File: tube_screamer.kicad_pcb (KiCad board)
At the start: 2 copper layers, 80 x 90 mm, 51 parts, among them J1 NMJ6HHD2, J2 NMJ6HHD2, J3 Conn_01x05, J4 Conn_01x05, J5 Conn_01x05, Q1 MMBT5551, Q2 MMBT5551, Q3 MMBT5551, SW1 SW_DPDT_x2, U1 NE5532

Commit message: Goin well.
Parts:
- removed TP11: input, TestPoint:TestPoint_THTPad_2.5x2.5mm_Drill1.2mm
- removed TP12: ground, TestPoint:TestPoint_THTPad_2.5x2.5mm_Drill1.2mm
- added BT1: Battery_Cell, pedale:BatteryHolder_Eagle_12BH611-GR, F.Cu at (70.8, 89.7)
- added D5: 1N4148WS, Diode_SMD:D_SOD-323, F.Cu at (35.5, 92.0)
- added D8: floating_green_led, pedale:floating_green_led, F.Cu at (74.0, 138.0)
- added D9: floating_red_led, pedale:floating_red_led, F.Cu at (106.0, 138.0)
- added H1: MountingHole, pedale:M3_hole_with_spacer, F.Cu at (55.0, 55.0)
- added H2: MountingHole, pedale:M3_hole_with_spacer, F.Cu at (125.0, 55.0)
- added H3: MountingHole, pedale:M3_hole_with_spacer, F.Cu at (55.0, 145.0)
- added H4: MountingHole, pedale:M3_hole_with_spacer, F.Cu at (90.0, 145.0)
- added H5: MountingHole, pedale:M3_hole_with_spacer, F.Cu at (125.0, 145.0)
- added J6: Barrel_Jack_MountingPin, Connector_BarrelJack:BarrelJack_GCT_DCJ200-10-A_Horizontal, F.Cu at (63.9, 103.3)
- added P1: tube_screamer_front_panel, pedale:tube_screamer_front_plate, F.Cu at (50.0, 50.0)
- added RV1: floating_pot_knob, pedale:floating_pot_knob, F.Cu at (34.4, 102.2)
- added RV5: floating_pot, pedale:floating_pot, F.Cu at (34.4, 100.7)
- added RV6: floating_pot, pedale:floating_pot, F.Cu at (32.9, 102.2)
- added RV7: floating_pot_knob, pedale:floating_pot_knob, F.Cu at (32.9, 100.7)
- added RV8: floating_pot, pedale:floating_pot, F.Cu at (31.4, 102.2)
- added RV9: floating_pot_knob, pedale:floating_pot_knob, F.Cu at (31.4, 100.7)
- added SIM1: Logo_Open_Hardware_Small, Symbol:OSHW-Logo2_7.3x6mm_SilkScreen, F.Cu at (108.0, 145.0)
- moved C11 70.7 mm to (97.4, 65.0)
- moved C6 70.7 mm to (95.4, 58.8)
- moved D3 70.7 mm to (112.8, 66.0)
- moved R19 70.7 mm to (87.4, 65.3)
- moved C1 70.7 mm to (64.3, 62.9)
- moved C10 70.7 mm to (63.5, 68.6)
- moved C14 70.7 mm to (124.0, 60.4)
- moved C16 70.7 mm to (115.6, 75.9)
- moved C17 70.7 mm to (124.9, 66.2)
- moved C18 70.7 mm to (108.6, 67.4)
- moved C3 70.7 mm to (68.0, 69.2)
- moved C5 70.7 mm to (72.0, 75.9)
- moved C9 70.7 mm to (55.7, 63.8)
- moved D1 70.7 mm to (68.0, 67.1)
- moved D2 70.7 mm to (68.0, 64.4)
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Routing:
- net Net-(D4-A): track 66.4 -> 68.7 mm
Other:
- board size 80 x 90 mm -> 80 x 100 mm

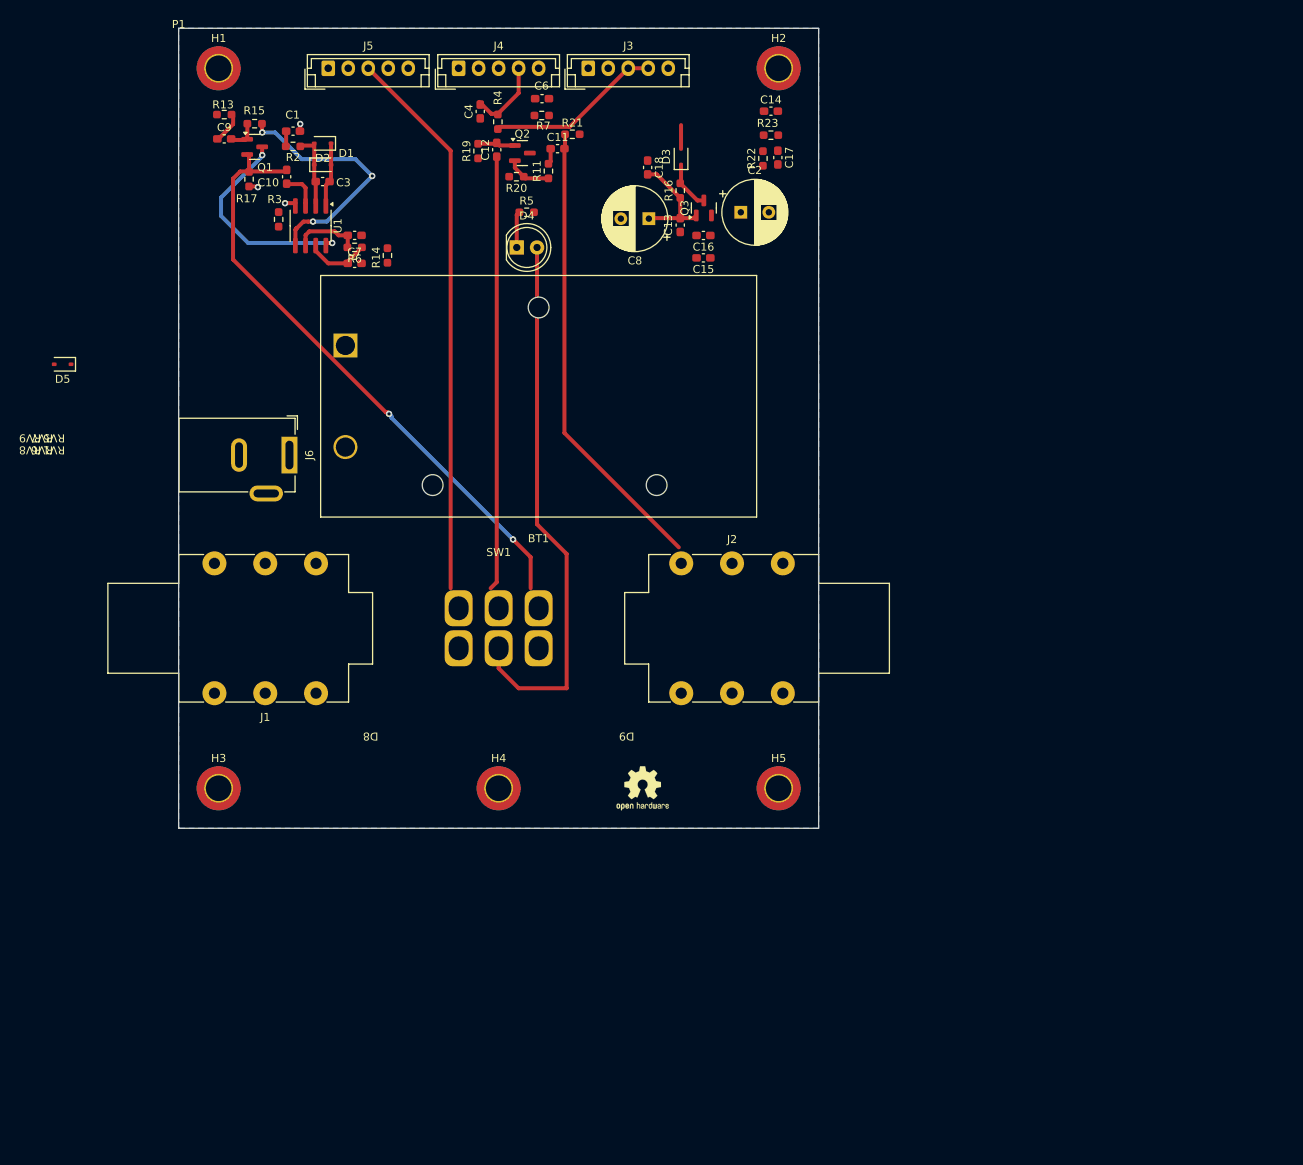
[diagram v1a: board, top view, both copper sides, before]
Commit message: 3D bodies
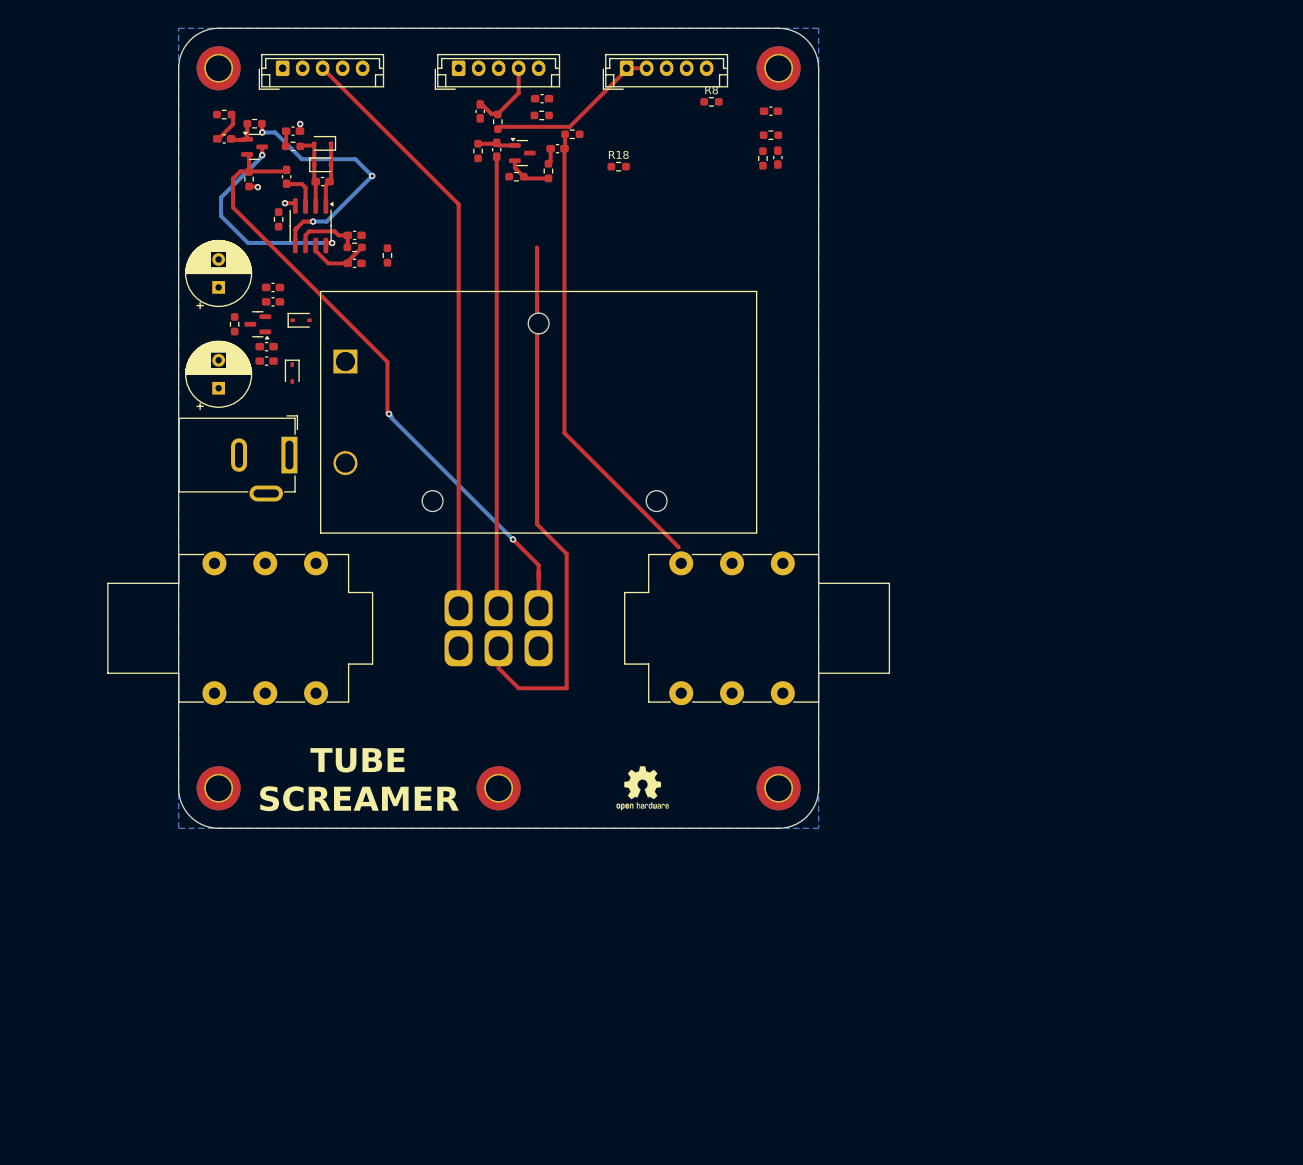
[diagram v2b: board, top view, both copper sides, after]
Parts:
- removed D4: LED, LED_THT:LED_D5.0mm
- removed R5: 1k, Resistor_SMD:R_0603_1608Metric_Pad0.98x0.95mm_HandSolder
- removed RV6: floating_pot, pedale:floating_pot
- added R18: 1k, Resistor_SMD:R_0603_1608Metric_Pad0.98x0.95mm_HandSolder, F.Cu at (105.0, 67.3)
- added R8: 1k, Resistor_SMD:R_0603_1608Metric_Pad0.98x0.95mm_HandSolder, F.Cu at (116.6, 59.2)
- moved RV1 87.4 mm to (112.0, 62.0), turned to 0 degrees
- moved C2 65.9 mm to (55.0, 82.4), turned to 90 degrees
- moved RV8 63.4 mm to (90.0, 78.0)
- moved RV7 61.8 mm to (90.0, 77.0), turned to 0 degrees
- moved R16 58.2 mm to (57.0, 87.0)
- moved C8 57.8 mm to (55.0, 95.0), turned to 90 degrees
- moved Q3 57.6 mm to (59.9, 87.0), turned to 180 degrees
- moved D3 55.6 mm to (64.2, 93.1), turned to -90 degrees
- moved C16 54.2 mm to (61.8, 82.4), turned to 0 degrees
- moved C15 54.1 mm to (61.8, 84.2), turned to 0 degrees
- moved C13 53.9 mm to (61.0, 89.8), turned to 0 degrees
- moved C18 53.4 mm to (61.0, 91.6), turned to 180 degrees
- moved RV9 53.3 mm to (68.0, 62.0), turned to 0 degrees
- moved RV5 50.5 mm to (68.0, 63.0), turned to 0 degrees
- moved D5 30.3 mm to (65.3, 86.5), turned to 0 degrees
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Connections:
- C4 pad 2: Net-(J4-Pin_4) -> Net-(J4-Pin_1)
- C5 pad 1: Net-(J4-Pin_4) -> Net-(J4-Pin_1)
- C5 pad 2: Net-(J4-Pin_2) -> Net-(J4-Pin_3)
- C6 pad 1: Net-(J4-Pin_3) -> Net-(J4-Pin_2)
- J3 pad 1: 0 -> Net-(D1-K)
- J3 pad 2: Net-(D1-K) -> Net-(D1-A)
- J3 pad 4: Net-(D1-A) -> 9V
- J3 pad 5: 0 -> Net-(J3-Pin_5)
- J4 pad 1: 0 -> Net-(J4-Pin_1)
- J4 pad 4: Net-(J4-Pin_4) -> unconnected-(J4-Pin_4-Pad4)
- J4 pad 5: 0 -> unconnected-(J4-Pin_5-Pad5)
- J5 pad 2: 0 -> /SW_ON
- J5 pad 3: /SW_ON -> Net-(J5-Pin_3)
- J5 pad 5: 0 -> Net-(J5-Pin_5)
- R14 pad 1: Net-(J5-Pin_4) -> Net-(J5-Pin_3)
- R4 pad 1: Net-(J4-Pin_4) -> Net-(J4-Pin_1)
- R6 pad 2: Net-(J4-Pin_2) -> Net-(J4-Pin_3)
- SW1 pad 5: Net-(D4-A) -> Net-(J5-Pin_4)
- U1 pad 6: Net-(J4-Pin_2) -> Net-(J4-Pin_3)
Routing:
- net Net-(J5-Pin_4): track 0.00 -> 68.7 mm
- net Net-(D4-A): track 68.7 -> 0.00 mm
- net Net-(Q3-B): track 13.9 -> 0.00 mm
- net Net-(J4-Pin_4): track 9.70 -> 0.00 mm
- net Net-(J4-Pin_1): track 0.00 -> 9.70 mm
- net Net-(J4-Pin_3): track 0.00 -> 8.17 mm
- net Net-(J4-Pin_2): track 8.17 -> 0.00 mm
- net Net-(D3-K): track 6.16 -> 0.00 mm
- net /SW_ON: track 69.3 -> 74.5 mm
- net Net-(D4-K): track 4.54 -> 0.00 mm
- net IN_BUFF: track 76.2 -> 80.0 mm
- net Net-(D3-A): track 2.90 -> 0.00 mm
- net /SW_MID: track 54.3 -> 56.5 mm
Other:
- outline, holes or cut-outs redrawn
- board text added: "TUBE SCREAMER"

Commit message: v1.
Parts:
- added RV6: floating_pot, pedale:floating_pot, F.Cu at (112.0, 63.0)
- moved R13 53.4 mm to (106.8, 76.5), turned to -90 degrees
- moved C7 50.3 mm to (119.2, 62.0), turned to 90 degrees
- moved C9 50.0 mm to (105.0, 72.6), turned to -90 degrees
- moved R6 48.7 mm to (119.2, 65.8), turned to -90 degrees
- moved R15 47.7 mm to (105.0, 76.3), turned to 90 degrees
- moved R3 47.3 mm to (109.5, 68.8), turned to 0 degrees
- moved U1 47.2 mm to (112.5, 64.2), turned to 0 degrees
- moved Q1 43.7 mm to (102.0, 75.1), turned to -90 degrees
- moved C10 41.7 mm to (105.2, 68.5), turned to 0 degrees
- moved R17 39.5 mm to (97.9, 74.4), turned to 180 degrees
- moved C3 38.2 mm to (105.8, 64.0), turned to 90 degrees
- moved C1 36.6 mm to (100.5, 68.7)
- moved R2 36.2 mm to (100.5, 66.8)
- moved D1 35.9 mm to (103.7, 64.0), turned to 90 degrees
- moved D2 33.2 mm to (101.2, 63.8), turned to -90 degrees
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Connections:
- net Net-(J5-Pin_3) renamed OP_OUT
- J1 pad S: unconnected-(J1-PadS) -> 0
- J2 pad S: unconnected-(J2-PadS) -> 0
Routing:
- net Net-(J1-PadT): track 0.00 -> 98.4 mm, vias 0 -> 2
- net Net-(J5-Pin_4): track 68.7 -> 126.2 mm
- net Net-(C7-Pad2): track 0.00 -> 54.3 mm, vias 0 -> 4
- net 4V5: track 31.2 -> 0.00 mm, vias 3 -> 0
- net 9V: track 26.9 -> 3.25 mm, vias 2 -> 1
- net IN_BUFF: track 80.0 -> 59.0 mm
- net Net-(Q3-B): track 0.00 -> 13.7 mm
- net Net-(D3-K): track 0.00 -> 13.6 mm
- net Net-(D1-K): track 9.08 -> 20.7 mm, vias 0 -> 1
- net Net-(D3-A): track 0.00 -> 9.34 mm
- net Net-(J4-Pin_3): track 8.17 -> 16.9 mm
- net Net-(D1-A): track 29.7 -> 37.6 mm
- net Net-(BT1-+): track 0.00 -> 7.01 mm
- net Net-(J4-Pin_1): track 9.70 -> 16.7 mm
- net Net-(J5-Pin_5): track 0.00 -> 6.49 mm
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
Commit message: v2.
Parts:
- moved R17 29.2 mm to (127.1, 74.9), turned to -90 degrees
- moved C7 28.1 mm to (93.1, 72.2), turned to -90 degrees
- moved R14 26.4 mm to (91.3, 72.3)
- moved R6 26.3 mm to (93.1, 68.7), turned to 90 degrees
- moved Q1 22.0 mm to (124.0, 74.8), turned to 180 degrees
- moved C17 21.3 mm to (97.0, 73.7)
- moved C9 21.3 mm to (125.3, 78.8), turned to 90 degrees
- moved C4 20.4 mm to (103.0, 74.7), turned to -90 degrees
- moved R15 17.7 mm to (122.6, 77.9), turned to 0 degrees
- moved R4 16.4 mm to (101.4, 74.7), turned to 90 degrees
- moved R13 16.2 mm to (122.6, 79.7), turned to 180 degrees
- moved U1 14.0 mm to (99.8, 70.1), turned to 180 degrees
- moved C5 13.0 mm to (99.8, 74.7), turned to 90 degrees
- moved R2 12.5 mm to (112.2, 71.1), turned to 180 degrees
- moved C1 12.4 mm to (112.2, 72.8), turned to 0 degrees
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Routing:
- net Net-(C11-Pad2): track 54.7 -> 0.00 mm
- net Net-(C7-Pad2): track 54.3 -> 1.86 mm, vias 4 -> 0
- net Net-(J5-Pin_4): track 126.2 -> 80.7 mm
- net IN_BUFF: track 59.0 -> 97.2 mm, vias 2 -> 0
- net OP_OUT: track 3.86 -> 39.5 mm
- net Net-(J4-Pin_1): track 16.7 -> 35.6 mm, vias 0 -> 2
- net Net-(J4-Pin_3): track 16.9 -> 25.0 mm
- net Net-(U1A-+): track 7.96 -> 0.00 mm
- net Net-(Q2-E): track 5.64 -> 0.00 mm
- net Net-(D1-A): track 37.6 -> 32.4 mm
- net Net-(J4-Pin_2): track 5.02 -> 0.00 mm
- net Net-(J1-PadT): track 98.4 -> 103.1 mm
- net Net-(Q1-B): track 4.31 -> 0.00 mm
- net Net-(J3-Pin_5): track 4.29 -> 0.00 mm
- net Net-(C9-Pad1): track 5.64 -> 1.80 mm
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
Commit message: povezano
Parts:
- moved C14 20.6 mm to (113.2, 77.9), turned to -90 degrees
- moved R23 20.1 mm to (110.2, 77.9), turned to -90 degrees
- moved R22 19.0 mm to (107.3, 76.9), turned to 0 degrees
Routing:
- net 9V: track 0.00 -> 194.5 mm, vias 0 -> 9
- net 4V5: track 0.00 -> 74.5 mm, vias 0 -> 5
- net Net-(C11-Pad2): track 0.00 -> 51.7 mm
- net 0: track 0.00 -> 20.7 mm, vias 0 -> 16
- net Net-(D1-K): track 19.4 -> 28.5 mm
- net Net-(D1-A): track 32.4 -> 39.8 mm
- net Net-(U1A-+): track 0.00 -> 4.82 mm
- net Net-(J3-Pin_5): track 0.00 -> 4.29 mm
- net Net-(J4-Pin_2): track 0.00 -> 4.20 mm
- net Net-(Q1-B): track 0.00 -> 4.14 mm
- net Net-(Q2-E): track 0.00 -> 3.46 mm
- net Net-(C11-Pad1): track 0.00 -> 2.53 mm
- net Net-(C6-Pad2): track 0.00 -> 1.82 mm
- net Net-(C1-Pad2): track 0.00 -> 1.72 mm

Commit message: Schematic fix, PCB final
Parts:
- removed C5: 100n, Capacitor_SMD:C_0603_1608Metric_Pad1.08x0.95mm_HandSolder
- added R25: 10k, Resistor_SMD:R_0603_1608Metric_Pad0.98x0.95mm_HandSolder, F.Cu at (97.0, 65.7)
- added R47: 47k, Resistor_SMD:R_0603_1608Metric_Pad0.98x0.95mm_HandSolder, F.Cu at (105.1, 59.0)
- added R48: 100, Resistor_SMD:R_0603_1608Metric_Pad0.98x0.95mm_HandSolder, F.Cu at (109.5, 69.1)
- moved R22 8.71 mm to (116.0, 77.1), turned to -90 degrees
- moved C14 1.04 mm to (113.5, 78.9)
- moved R23 1.04 mm to (110.5, 78.9)
- moved C6 0.40 mm to (87.5, 59.9)
- moved R7 0.40 mm to (85.7, 59.9)
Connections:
- C10 pad 1: IN_BUFF -> Net-(C10-Pad1)
- J3 pad 1: Net-(D1-K) -> Net-(J3-Pin_1)
- U1 pad 5: 4V5 -> Net-(J4-Pin_1)
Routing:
- net Net-(J4-Pin_3): track 25.0 -> 19.0 mm
- net Net-(D1-K): track 28.5 -> 23.5 mm
- net 9V: track 194.5 -> 190.4 mm, vias 9 -> 4
- net Net-(J3-Pin_1): track 0.00 -> 4.01 mm
- net IN_BUFF: track 97.2 -> 93.7 mm
- net Net-(C10-Pad1): track 0.00 -> 1.70 mm
- net Net-(Q3-B): track 13.7 -> 15.2 mm
- net Net-(J5-Pin_4): track 80.7 -> 82.1 mm
- net 4V5: track 74.5 -> 73.4 mm
- net Net-(J4-Pin_1): track 35.6 -> 35.1 mm
- net 0: track 20.7 -> 20.4 mm, vias 16 -> 154
- added copper zone on F.Cu, net 0

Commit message: All errors removed
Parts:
- removed RV1, RV7, RV9: floating_pot_knob, pedale:floating_pot_knob
- added J7: Conn_01x01_Socket, TestPoint:TestPoint_THTPad_D2.5mm_Drill1.2mm, F.Cu at (69.2, 89.6)
- added J8: Conn_01x01_Socket, TestPoint:TestPoint_THTPad_D2.5mm_Drill1.2mm, F.Cu at (69.2, 102.3)
- J1, J2: value NMJ6HHD2 -> Jack_6.35; footprint Connector_Audio:Jack_6.35mm_Neutrik_NMJ6HHD2_Horizontal -> pedale:Jack_6.35mm
- J6: value Barrel_Jack_MountingPin -> Barrel_Jack_Switch; footprint Connector_BarrelJack:BarrelJack_GCT_DCJ200-10-A_Horizontal -> pedale:BarrelJack
- SW1: value SW_DPDT_x2 -> pedala_switch; footprint switch:switch_DPDT -> pedale:foot_switch_tht_and_floating
- moved SW1 5.59 mm to (90.0, 125.0)
- moved BT1 4.61 mm to (75.0, 89.7)
- moved C14 1.00 mm to (113.5, 77.9)
- moved R22 1.00 mm to (116.0, 76.1)
- moved R23 1.00 mm to (110.5, 77.9)
- moved R13 0.65 mm to (122.6, 79.0)
- moved R15 0.65 mm to (122.6, 77.2)
- moved R17 0.65 mm to (127.1, 74.2)
- moved C9 0.65 mm to (125.3, 78.2)
- moved Q1 0.65 mm to (124.0, 74.2)
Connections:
- BT1 pad 2: 0 -> Net-(BT1--)
- J6 pad 3: (no net) -> Net-(BT1--)
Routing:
- net Net-(J1-PadT): track 103.1 -> 121.7 mm
- net Net-(BT1--): track 0.00 -> 17.5 mm
- net IN_BUFF: track 93.7 -> 87.1 mm, vias 0 -> 2
- net Net-(J5-Pin_4): track 82.1 -> 85.7 mm
- net /SW_ON: track 75.6 -> 72.2 mm
- net Net-(BT1-+): track 7.01 -> 10.1 mm
- net 9V: track 190.4 -> 189.2 mm, vias 4 -> 6
- net 0: track 20.4 -> 20.5 mm, vias 154 -> 86
